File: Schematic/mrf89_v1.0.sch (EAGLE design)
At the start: 20 parts, among them Q1 FC-12M, U1 MSP430FR5969, U5 MRF89XAM8A

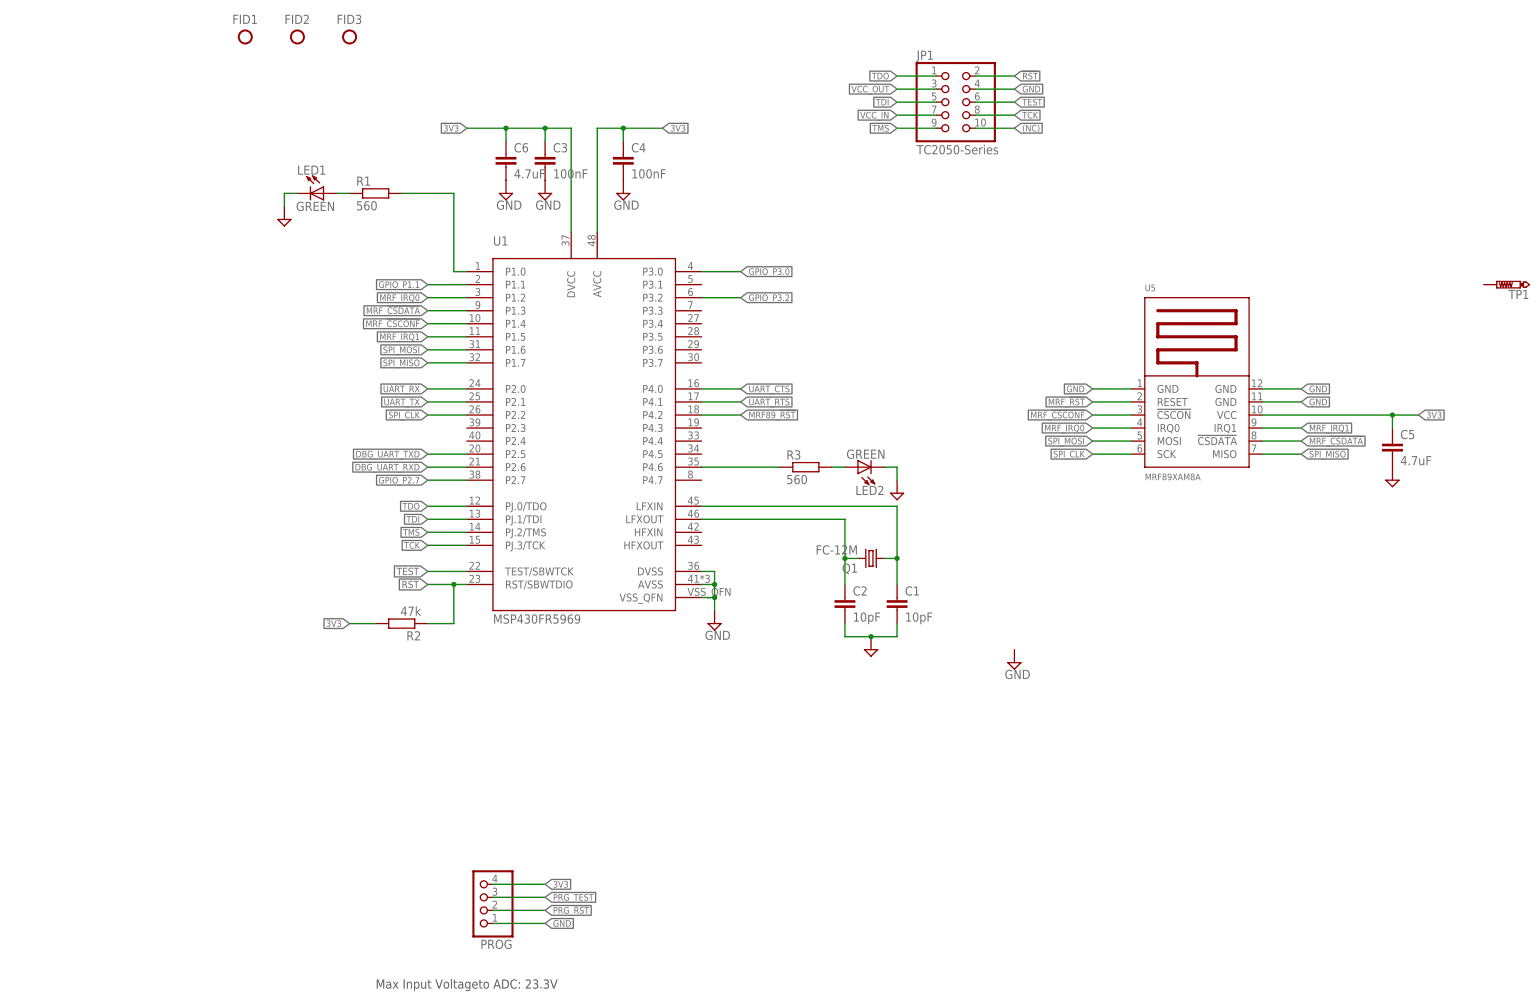
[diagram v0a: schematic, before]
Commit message: Finalized version 1.0
Finalized version of schematic and PCB.
Version 1.0
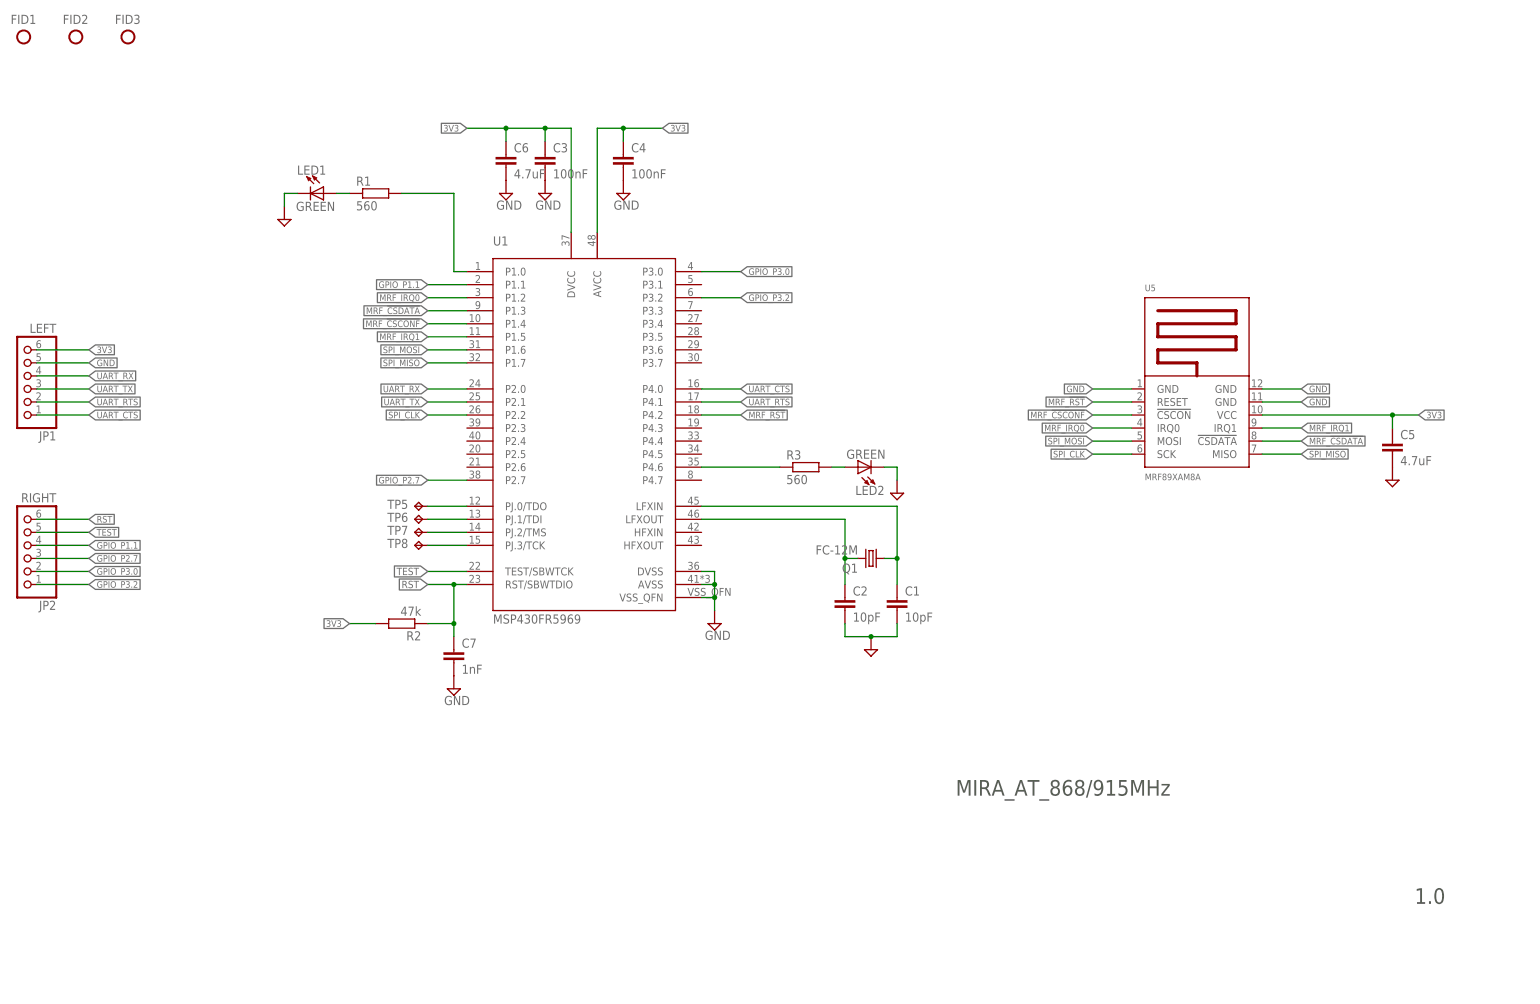
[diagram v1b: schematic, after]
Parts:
- removed PROG: (no value), pinhead:PINHD-1X4
- removed TP1: PTR1PAD1-13, testpad:PTR1PAD1-13
- added C7: 1nF, rcl:C-EUC0603
- added JP2: RIGHT, pinhead:PINHD-1X6
- added TP5, TP6, TP7, TP8: TPB1,27, testpad:TPB1,27
- JP1: value TC2050-Series -> LEFT; device pinhead:PINHD-2X5 -> pinhead:PINHD-1X6
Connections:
- net N$1 renamed LFXIN
- net N$16 renamed P1.0
- net N$2 renamed LFXOUT
- net N$4 renamed P4.6
- removed net !RST: JP1.2
- removed net (NC): JP1.10
- removed net DBG_UART_RXD: U1.P2.6
- removed net DBG_UART_TXD: U1.P2.5
- removed net MRF89_!RST: U1.P4.2
- removed net PRG_!RST: PROG.2
- removed net PRG_TEST: PROG.3
- removed net VCC_IN: JP1.7
- removed net VCC_OUT: JP1.3
- net 3V3: now also JP1.6; no longer PROG.4
- net GND: now also C7.2, JP1.5; no longer JP1.4, PROG.1
- net GPIO_P1.1: now also JP2.4
- net GPIO_P2.7: now also JP2.3
- net GPIO_P3.0: now also JP2.2
- net GPIO_P3.2: now also JP2.1
- net MRF_!RST: now also U1.P4.2
- net RST: now also C7.1, JP2.6
- net TCK: now also TP8.TP; no longer JP1.8
- net TDI: now also TP6.TP; no longer JP1.5
- net TDO: now also TP5.TP; no longer JP1.1
- net TEST: now also JP2.5; no longer JP1.6
- net TMS: now also TP7.TP; no longer JP1.9
- net UART_CTS: now also JP1.1
- net UART_RTS: now also JP1.2
- net UART_RX: now also JP1.4
- net UART_TX: now also JP1.3
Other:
- note added: "1.0"
- note added: "MIRA_AT_868/915MHz"
- note removed: "Max Input Voltageto ADC: 23.3V"
- moved on the sheet: FID1, FID2, FID3
